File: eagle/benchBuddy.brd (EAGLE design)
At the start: 114 x 76.2 mm, 104 parts, among them IC2 TLC274D, IC3 LM334Z, IC4 LM324D, IC5 LM324D, J1 12V_DC, J4 GND, J5 3.3V, J6 5V, J7 12V, J8 GND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

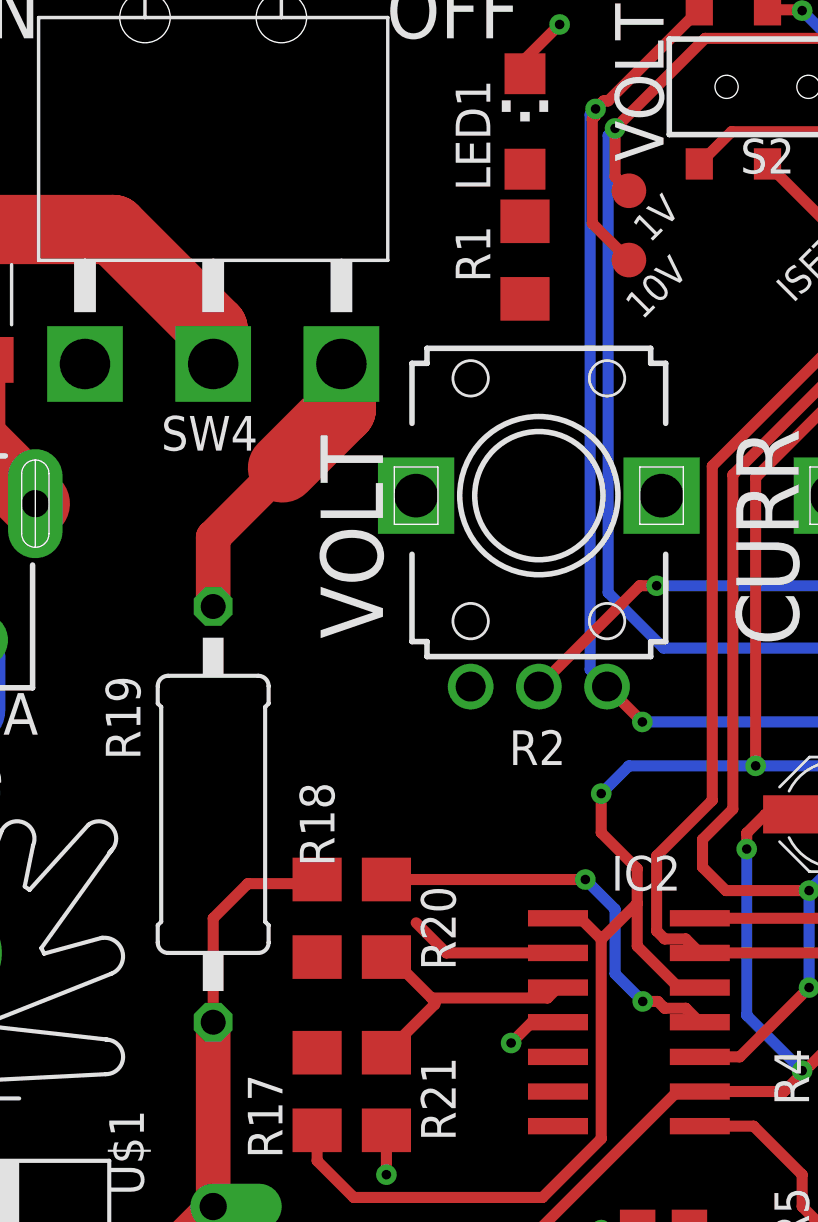
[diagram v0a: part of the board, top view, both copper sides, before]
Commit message: Fixed minor airwire issues
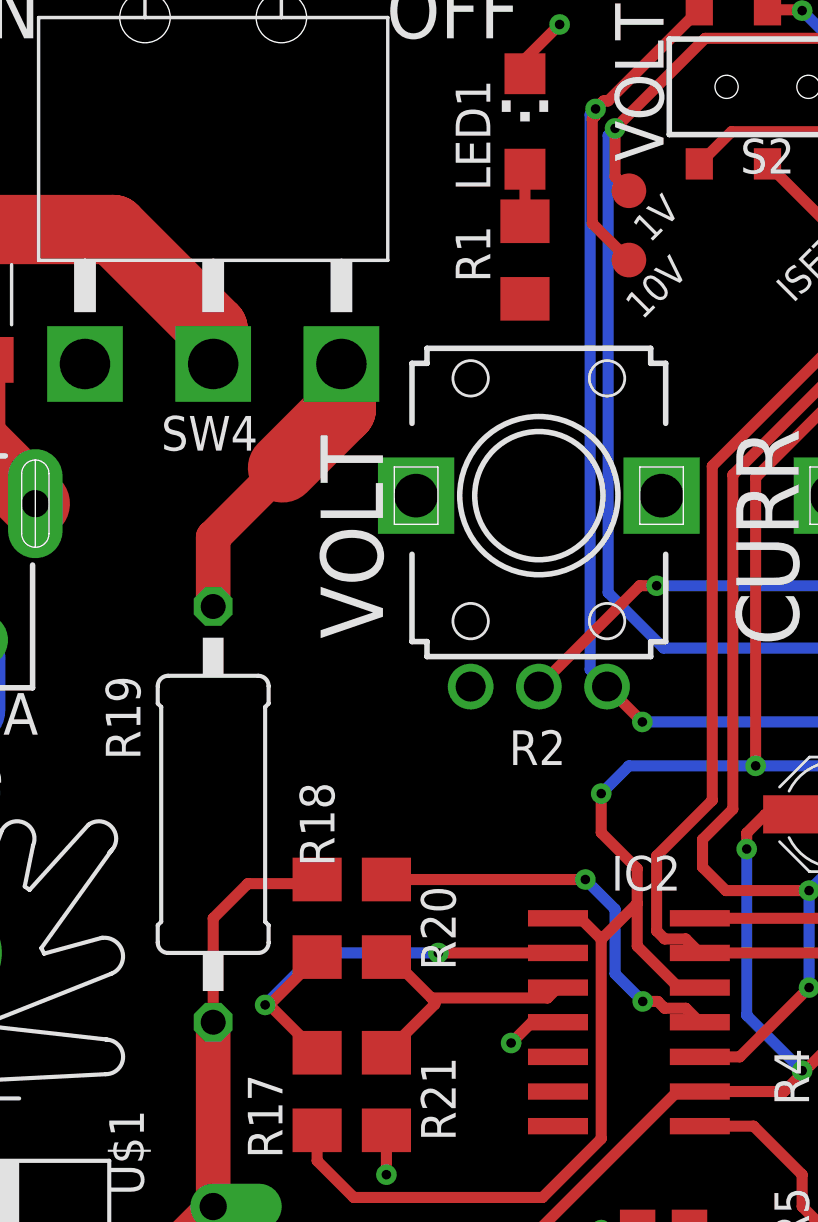
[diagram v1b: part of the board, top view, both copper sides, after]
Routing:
- net N$18: track 5.66 -> 16.6 mm, vias 0 -> 2
- net N$1: track 0.00 -> 1.91 mm
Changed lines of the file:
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@@
 <grid distance="25" unitdist="mil" unit="mil" style="lines" multiple="4" display="yes" altdistance="12.5" altunitdist="mil" altunit="mil"/>
 <layers>
-<layer number="1" name="Top" color="4" fill="1" visible="no" active="yes"/>
+<layer number="1" name="Top" color="4" fill="1" visible="yes" active="yes"/>
 <layer number="2" name="Route2" color="1" fill="3" visible="no" active="no"/>
 <layer number="3" name="Route3" color="4" fill="3" visible="no" active="no"/>
@@
 <layer number="14" name="Route14" color="1" fill="6" visible="no" active="no"/>
 <layer number="15" name="Route15" color="4" fill="6" visible="no" active="no"/>
-<layer number="16" name="Bottom" color="1" fill="1" visible="no" active="yes"/>
+<layer number="16" name="Bottom" color="1" fill="1" visible="yes" active="yes"/>
 <layer number="17" name="Pads" color="2" fill="1" visible="yes" active="yes"/>
 <layer number="18" name="Vias" color="2" fill="1" visible="yes" active="yes"/>
@@
 <layer number="20" name="Dimension" color="24" fill="1" visible="yes" active="yes"/>
 <layer number="21" name="tPlace" color="7" fill="1" visible="yes" active="yes"/>
-<layer number="22" name="bPlace" color="7" fill="1" visible="no" active="yes"/>
+<layer number="22" name="bPlace" color="7" fill="1" visible="yes" active="yes"/>
 <layer number="23" name="tOrigins" color="15" fill="1" visible="yes" active="yes"/>
-<layer number="24" name="bOrigins" color="15" fill="1" visible="no" active="yes"/>
+<layer number="24" name="bOrigins" color="15" fill="1" visible="yes" active="yes"/>
 <layer number="25" name="tNames" color="7" fill="1" visible="yes" active="yes"/>
-<layer number="26" name="bNames" color="7" fill="1" visible="no" active="yes"/>
+<layer number="26" name="bNames" color="7" fill="1" visible="yes" active="yes"/>
 <layer number="27" name="tValues" color="7" fill="1" visible="no" active="yes"/>
 <layer number="28" name="bValues" color="7" fill="1" visible="no" active="yes"/>
@@
 <layer number="37" name="tTest" color="7" fill="1" visible="no" active="yes"/>
 <layer number="38" name="bTest" color="7" fill="1" visible="no" active="yes"/>
-<layer number="39" name="tKeepout" color="4" fill="11" visible="no" active="yes"/>
-<layer number="40" name="bKeepout" color="1" fill="11" visible="no" active="yes"/>
-<layer number="41" name="tRestrict" color="4" fill="10" visible="no" active="yes"/>
-<layer number="42" name="bRestrict" color="1" fill="10" visible="no" active="yes"/>
+<layer number="39" name="tKeepout" color="4" fill="11" visible="yes" active="yes"/>
+<layer number="40" name="bKeepout" color="1" fill="11" visible="yes" active="yes"/>
+<layer number="41" name="tRestrict" color="4" fill="10" visible="yes" active="yes"/>
+<layer number="42" name="bRestrict" color="1" fill="10" visible="yes" active="yes"/>
 <layer number="43" name="vRestrict" color="2" fill="10" visible="no" active="yes"/>
 <layer number="44" name="Drills" color="7" fill="1" visible="no" active="yes"/>
@@
 <layer number="50" name="dxf" color="7" fill="1" visible="no" active="no"/>
 <layer number="51" name="tDocu" color="7" fill="1" visible="yes" active="yes"/>
-<layer number="52" name="bDocu" color="7" fill="1" visible="no" active="yes"/>
+<layer number="52" name="bDocu" color="7" fill="1" visible="yes" active="yes"/>
 <layer number="53" name="tGND_GNDA" color="7" fill="9" visible="no" active="no"/>
 <layer number="54" name="bGND_GNDA" color="1" fill="9" visible="no" active="no"/>
@@
 <contactref element="R1" pad="1"/>
 <contactref element="LED1" pad="A"/>
-<wire x1="30.48" y1="68.1" x2="30.48" y2="66.192" width="0" layer="19" extent="1-1"/>
+<wire x1="30.48" y1="68.1" x2="30.48" y2="66.192" width="0.4064" layer="1"/>
 </signal>
 <signal name="VCC">
@@
 <contactref element="R18" pad="1"/>
 <contactref element="R17" pad="1"/>
-<wire x1="31.69" y1="39.37" x2="27.59608125" y2="39.37" width="0.4064" layer="1"/>
-<wire x1="26.49088125" y1="40.4752" x2="27.59608125" y2="39.37" width="0.4064" layer="1"/>
-<wire x1="22.86" y1="39.218" x2="26.49088125" y2="40.4752" width="0" layer="19" extent="1-1"/>
-<wire x1="22.86" y1="35.712" x2="22.86" y2="39.218" width="0" layer="19" extent="1-1"/>
+<wire x1="22.86" y1="39.218" x2="21.107" y2="37.465" width="0.4064" layer="1"/>
+<via x="20.955" y="37.465" extent="1-16" drill="0.35"/>
+<wire x1="20.955" y1="37.465" x2="22.86" y2="39.37" width="0.4064" layer="16"/>
+<wire x1="22.86" y1="39.37" x2="27.305" y2="39.37" width="0.4064" layer="16"/>
+<via x="27.305" y="39.37" extent="1-16" drill="0.35"/>
+<wire x1="20.955" y1="37.465" x2="21.107" y2="37.465" width="0.4064" layer="1"/>
+<wire x1="21.107" y1="37.465" x2="22.86" y2="35.712" width="0.4064" layer="1"/>
+<wire x1="31.69" y1="39.37" x2="27.305" y2="39.37" width="0.4064" layer="1"/>
 </signal>
 <signal name="I_OUT">

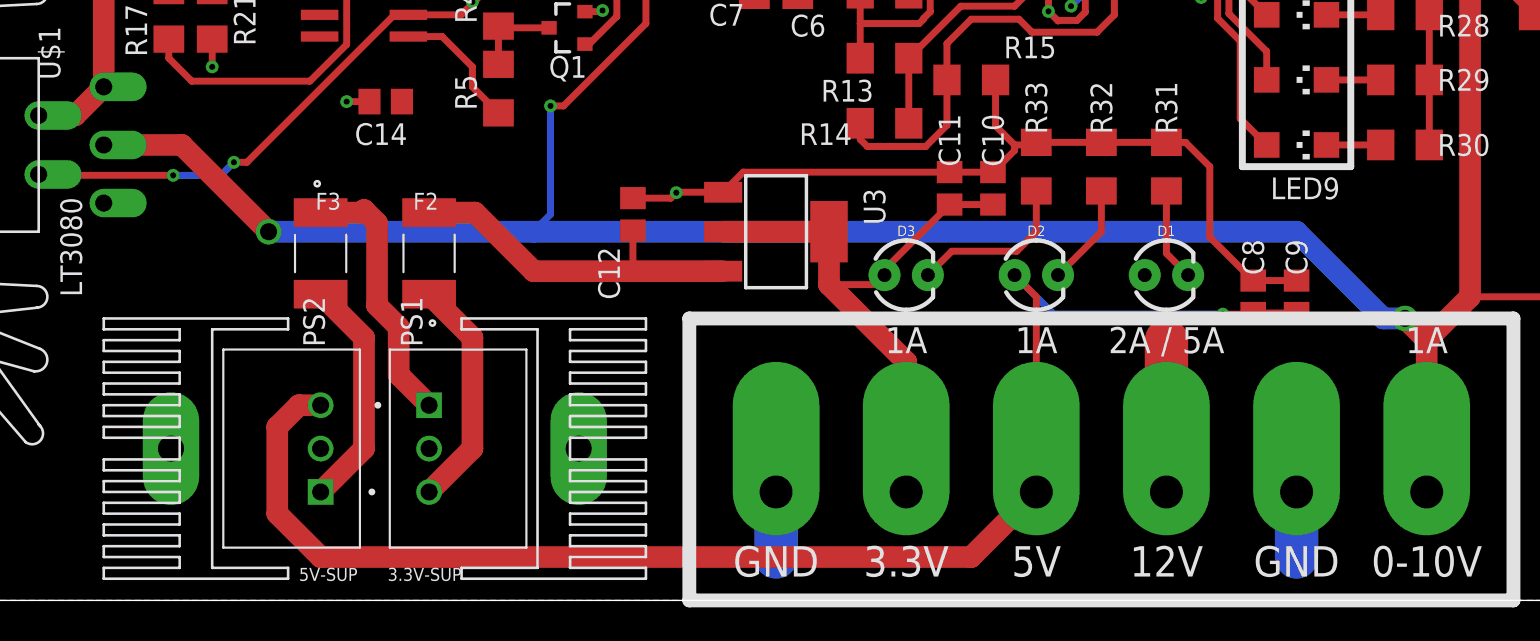
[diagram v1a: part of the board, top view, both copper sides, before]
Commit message: Rotated 5VRegs so that Heatsink faces edge
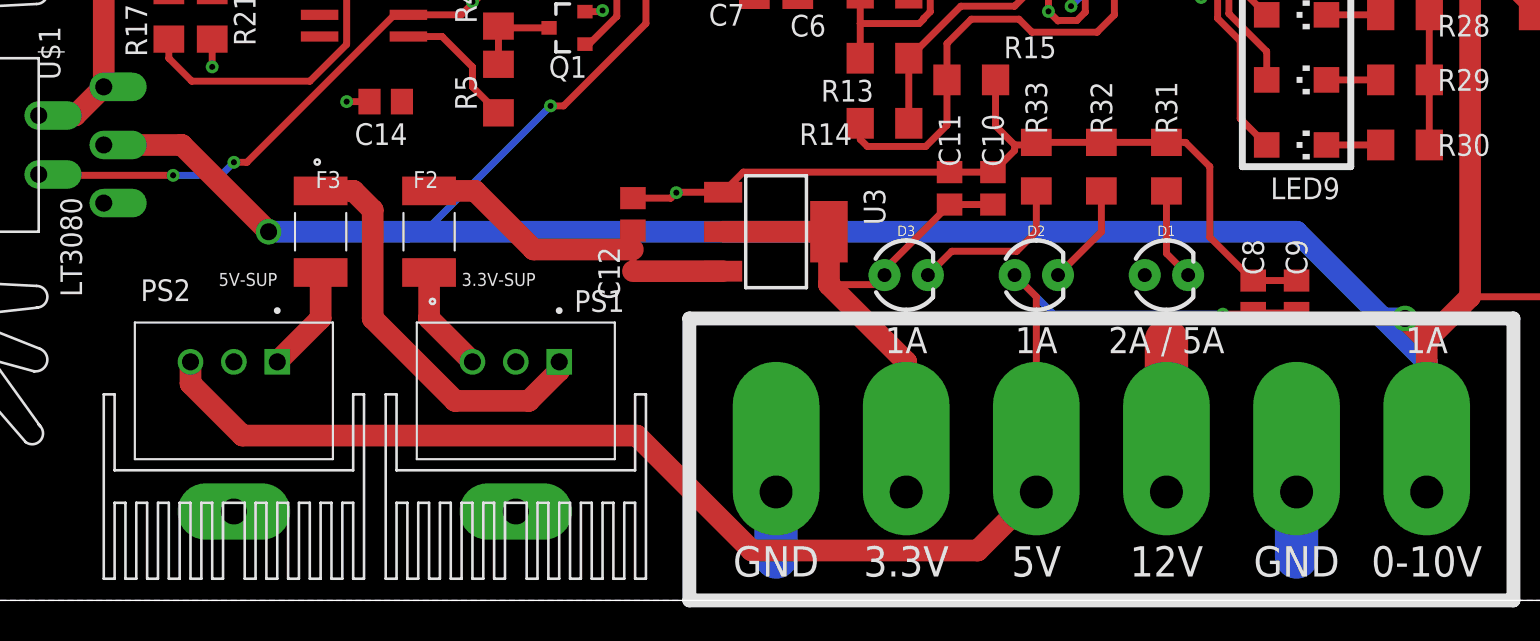
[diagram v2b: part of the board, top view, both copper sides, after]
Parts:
- moved PS1 7.18 mm to (43.2, 14.0), turned to 180 degrees
- moved PS2 7.18 mm to (26.7, 14.0), turned to 180 degrees
- moved U$2 1.80 mm to (43.2, 7.62), turned to 180 degrees
- moved U$3 1.80 mm to (26.7, 7.62), turned to 180 degrees
- moved F2 1.27 mm to (38.1, 21.6)
- moved F3 1.27 mm to (31.8, 21.6)
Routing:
- net VCC: track 259.3 -> 274.2 mm
- net VIN: track 86.7 -> 95.1 mm
- net N$7: track 13.7 -> 6.28 mm
- net N$48: track 13.7 -> 6.28 mm
- net 5V: track 85.9 -> 87.0 mm
